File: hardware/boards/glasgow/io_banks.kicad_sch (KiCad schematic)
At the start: 27 parts, among them J10 AUX, J4 Conn_01x02, J5 PinHeader_2x22_P1.27mm, U30 ICE40HX8K-BG121, U32 SN74LVC1T45DCKR

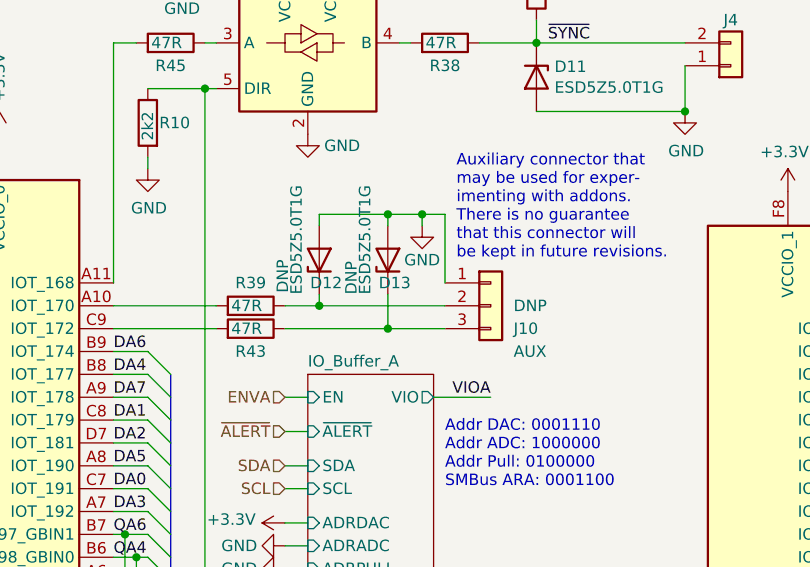
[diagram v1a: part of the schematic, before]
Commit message: revC3: Use the new KiCad DNP flag for the DNP parts.
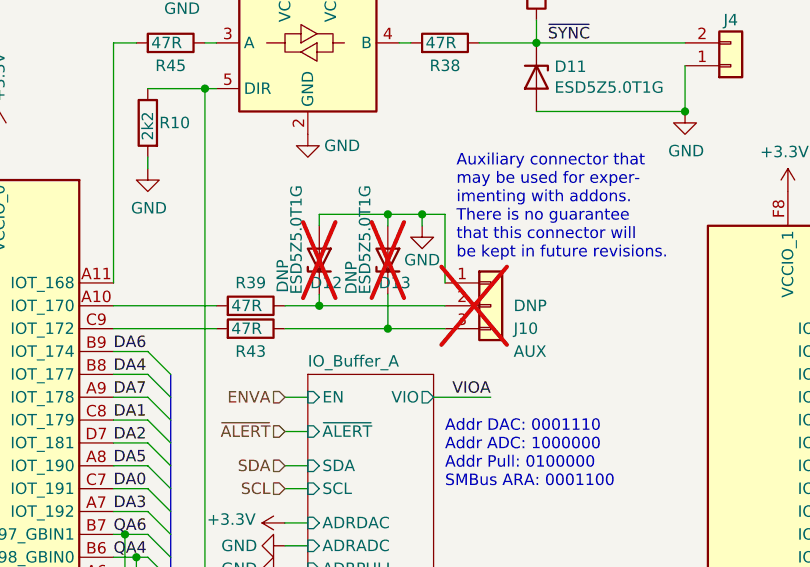
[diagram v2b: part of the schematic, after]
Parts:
- D12, D13, J10: now not fitted; now left out of the parts list
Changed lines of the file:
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@@
   )
   (symbol (lib_id "Connector_Generic:Conn_01x03") (at 87.63 90.17 0) (unit 1)
-    (in_bom yes) (on_board yes) (dnp no)
+    (in_bom no) (on_board yes) (dnp yes)
     (property "Reference" "J10" (at 90.17 92.71 0)
       (effects (font (size 1.27 1.27)) (justify left))
@@
   )
   (symbol (lib_id "Device:D_Zener") (at 68.58 85.09 90) (unit 1)
-    (in_bom yes) (on_board yes) (dnp no)
+    (in_bom no) (on_board yes) (dnp yes)
     (property "Reference" "D12" (at 71.12 87.63 90)
       (effects (font (size 1.27 1.27)) (justify left))
@@
   )
   (symbol (lib_id "Device:D_Zener") (at 76.2 85.09 90) (unit 1)
-    (in_bom yes) (on_board yes) (dnp no)
+    (in_bom no) (on_board yes) (dnp yes)
     (property "Reference" "D13" (at 78.74 87.63 90)
       (effects (font (size 1.27 1.27)) (justify left))

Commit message: revC3: Marked non schematic/bom parts correctly.
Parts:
- D12, D13, J10: now in the parts list
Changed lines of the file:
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@@
   )
   (symbol (lib_id "Connector_Generic:Conn_01x03") (at 87.63 90.17 0) (unit 1)
-    (in_bom no) (on_board yes) (dnp yes)
+    (in_bom yes) (on_board yes) (dnp yes)
     (property "Reference" "J10" (at 90.17 92.71 0)
       (effects (font (size 1.27 1.27)) (justify left))
@@
   )
   (symbol (lib_id "Device:D_Zener") (at 68.58 85.09 90) (unit 1)
-    (in_bom no) (on_board yes) (dnp yes)
+    (in_bom yes) (on_board yes) (dnp yes)
     (property "Reference" "D12" (at 71.12 87.63 90)
       (effects (font (size 1.27 1.27)) (justify left))
@@
   )
   (symbol (lib_id "Device:D_Zener") (at 76.2 85.09 90) (unit 1)
-    (in_bom no) (on_board yes) (dnp yes)
+    (in_bom yes) (on_board yes) (dnp yes)
     (property "Reference" "D13" (at 78.74 87.63 90)
       (effects (font (size 1.27 1.27)) (justify left))

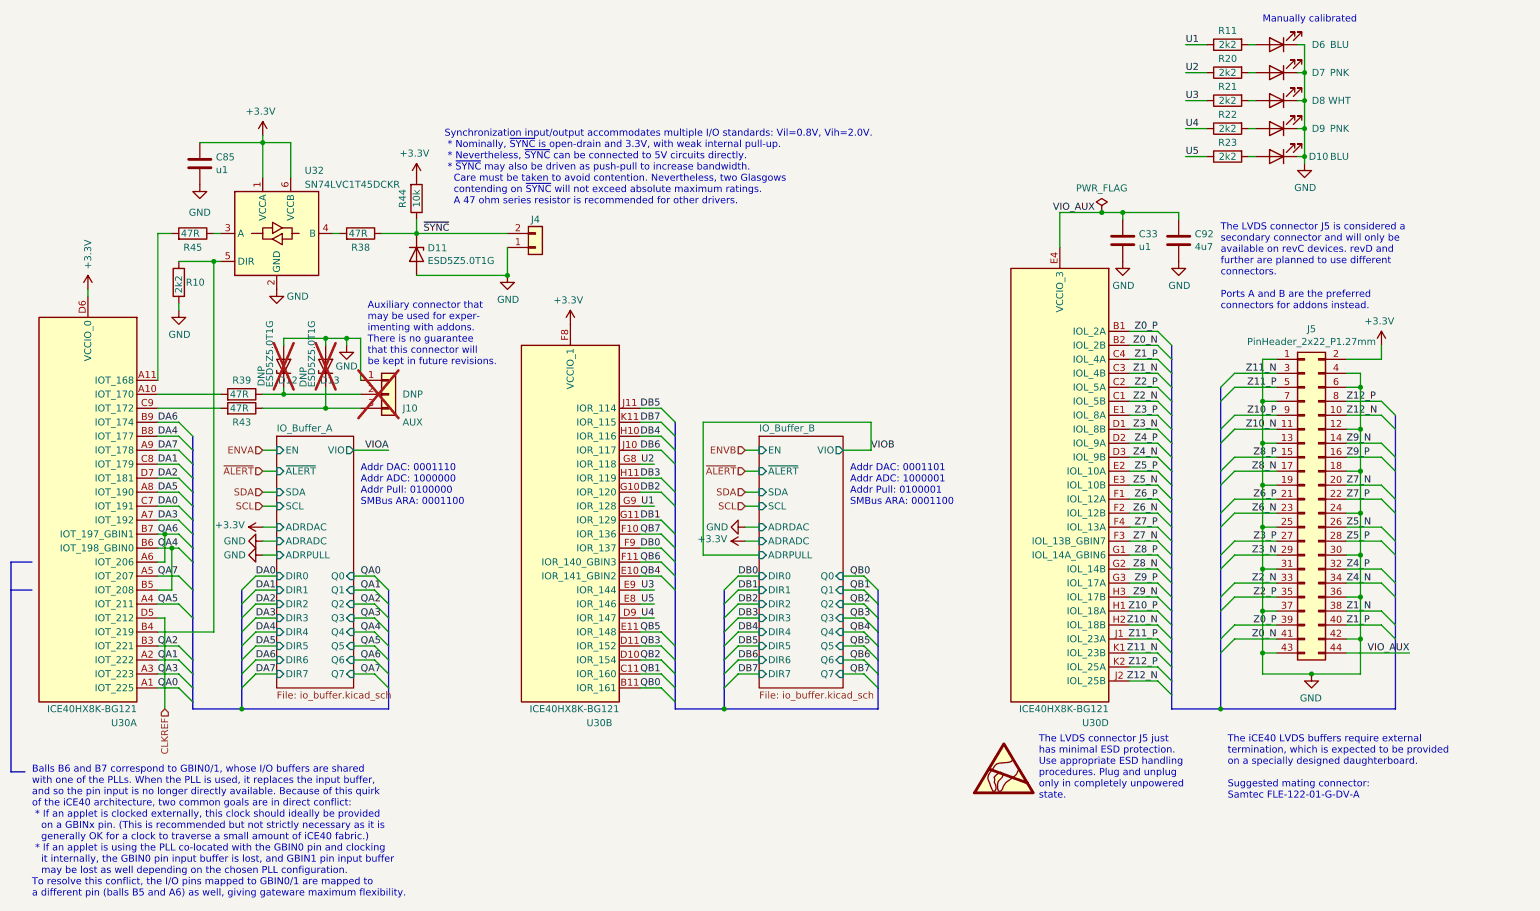
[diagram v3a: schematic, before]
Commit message: hardware: open & save with KiCAD 8.0.9
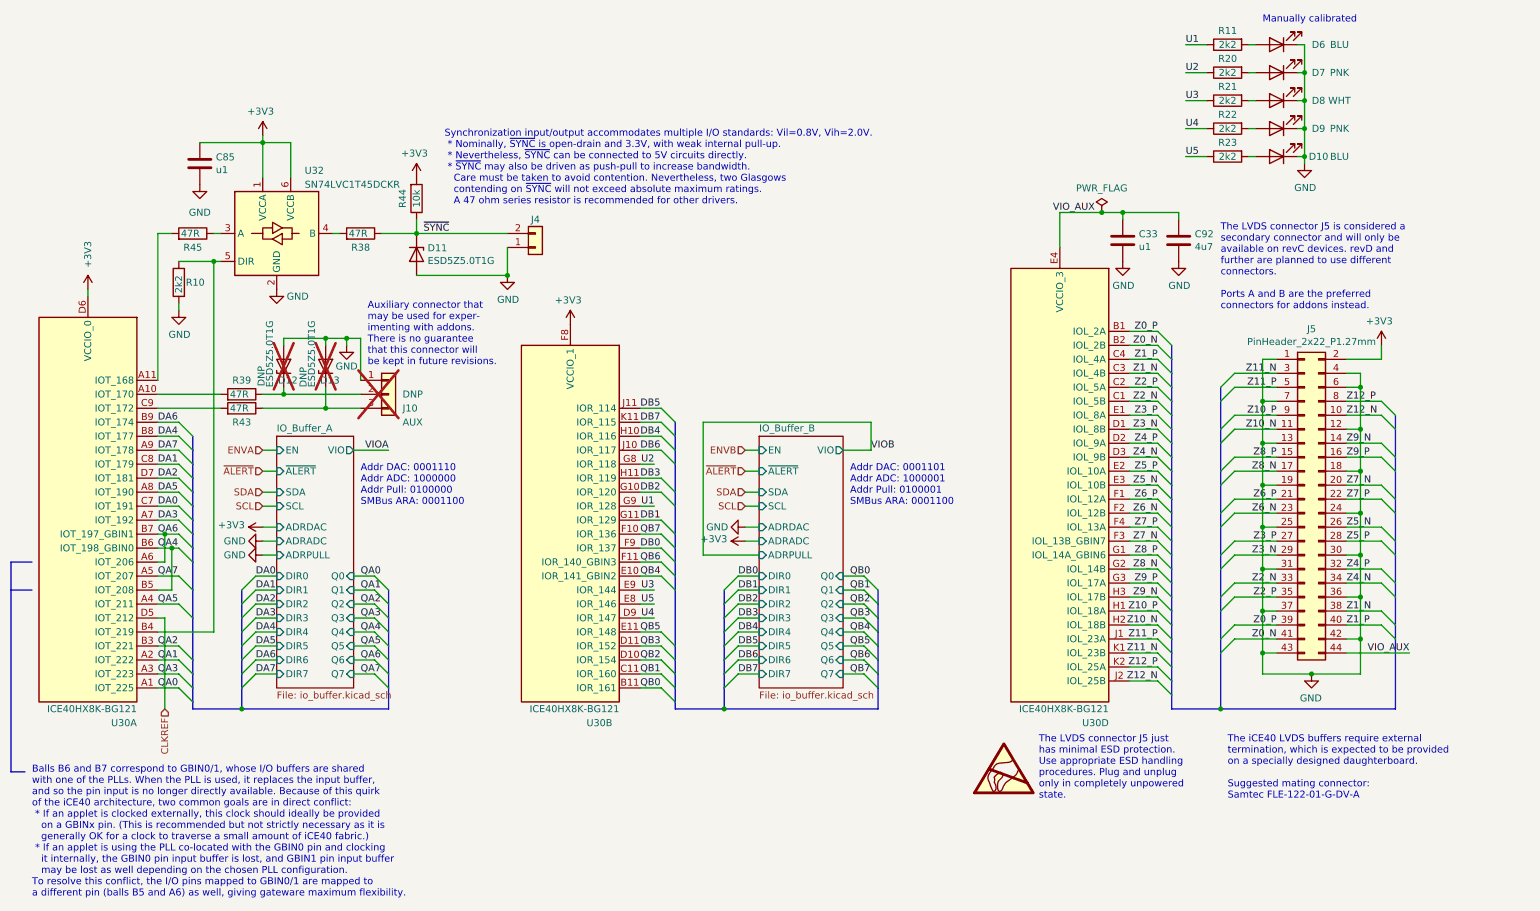
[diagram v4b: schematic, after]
